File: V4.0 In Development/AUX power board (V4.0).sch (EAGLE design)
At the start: 75 parts, among them U1 ATMEGA328P_TQFP, U2 TPS5405DR

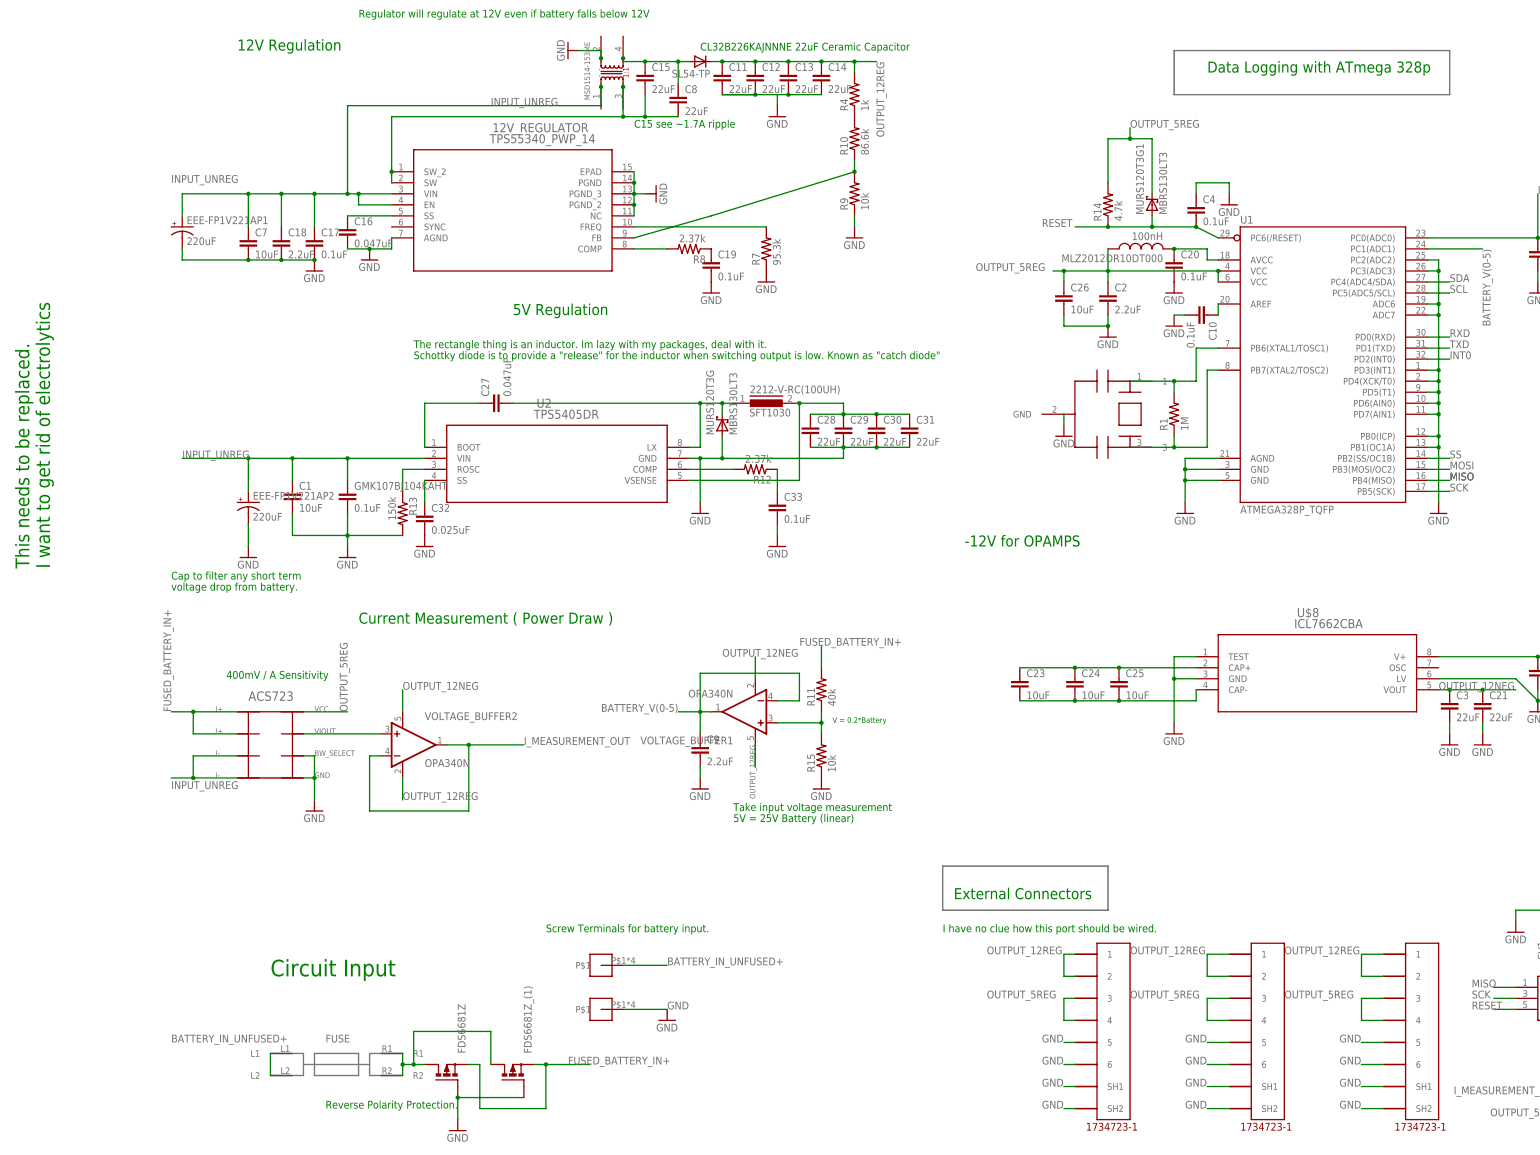
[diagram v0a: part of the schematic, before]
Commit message: Using nMOS reverse polarity protection
-added a cheaper 10uH inductor to the 5V supply
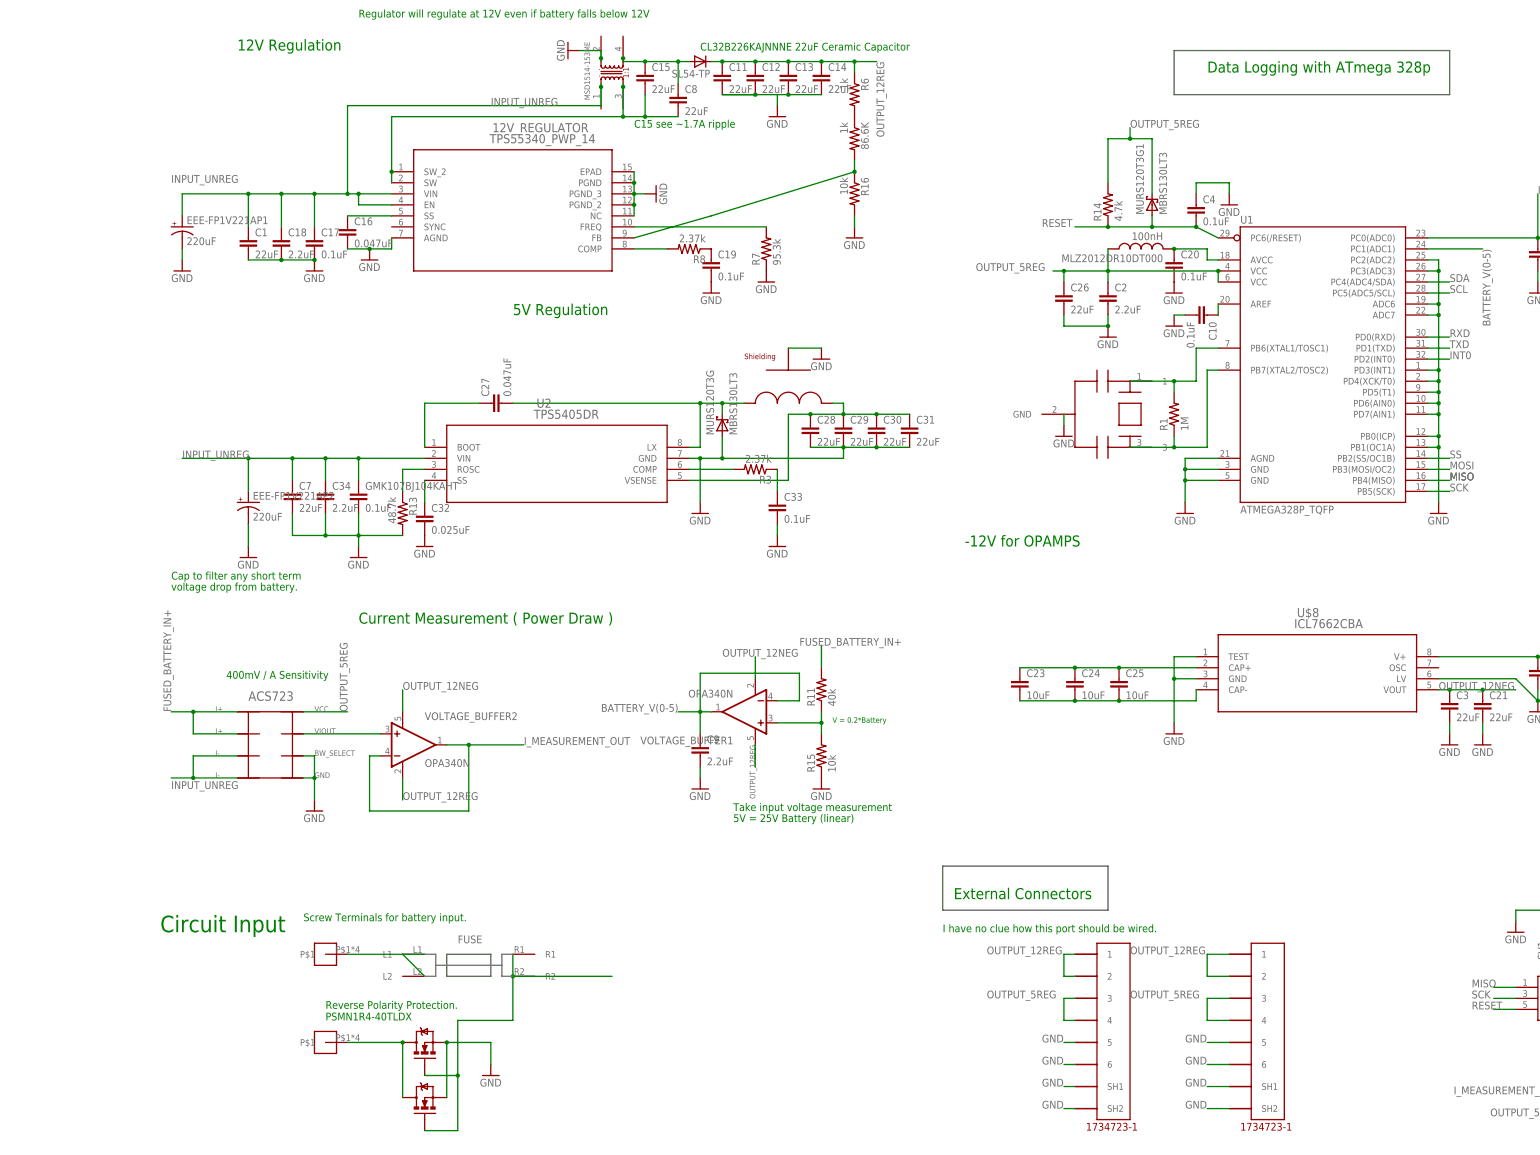
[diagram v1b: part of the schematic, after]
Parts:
- removed 2212-V-RC(100UH): SFT1030, inductors:SFT1030
- removed FDS6681Z, FDS6681Z_(1): (no value), transistor-power:P-MOSFET-SO8
- removed R10: 86.6k, resistor:R-US_R0603
- removed R4: 1k, resistor:R-US_R0603
- removed R9: 10k, resistor:R-US_R0603
- added 86.6K, R6: 1k, resistor:R-US_R0805
- added C34: 2.2uF, rcl:C-EUC0603
- added PSMN1R4-40TLDX, Q2: MOSFET-NCHANNELFDS6630A, PSMN1R4-40YLDX:MOSFET-NCHANNELFDS6630A
- added R16: 10k, resistor:R-US_R0805
- C1, C26, C7: value 10uF -> 22uF; device rcl:C-EUC0805 -> rcl:C-EUC1210
- R13: value 150k -> 48.7k
- U$5: value 5555140-6 -> CDEP147NP-100MC-125; device 5555140-6 RJ11:5555140-6 -> CDEP147NP-100MC-125:CDEP147NP-100MC-125
- renumbered R12 to R3
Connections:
- removed net MMM: FDS6681Z.D, FDS6681Z_(1).D, MINIBLADE.R1, MINIBLADE.R2
- removed net N$17: 2212-V-RC(100UH).2, C28.1, C29.1, C30.1, C31.1, U2.VSENSE
- new net N$22: PSMN1R4-40TLDX.D, Q2.D, U$7.P$1
- new net N$25: MINIBLADE.R1, MINIBLADE.R2, PSMN1R4-40TLDX.G, Q2.G
- new net N$26: C28.1, C29.1, C30.1, C31.1, U$5.PIN2, U2.VSENSE
- net FUSED_BATTERY_IN+: no longer FDS6681Z.S, FDS6681Z_(1).S
- net GND: now also C34.2, PSMN1R4-40TLDX.S, Q2.S, R16.2, U$5.GND; no longer FDS6681Z.G, FDS6681Z_(1).G, R9.1, U$5.5, U$5.6, U$5.SH1, U$5.SH2, U$7.P$1
- net INPUT_UNREG: now also C34.1
- net N$15: now also 86.6K.2, R16.1; no longer R10.1, R9.2
- net N$3: now also 86.6K.1, R6.2; no longer R10.2, R4.1
- net N$7: now also U$5.PIN1; no longer 2212-V-RC(100UH).1
- net OUTPUT_12REG: now also R6.1; no longer R4.2, U$5.1, U$5.2
- net OUTPUT_5REG: no longer U$5.3, U$5.4
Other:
- note added: "Reverse Polarity Protection. PSMN1R4-40TLDX"
- note removed: "Reverse Polarity Protection."
- note removed: "Schottky diode is to provide a "release" for the inductor when switching output is low. Known as "catch diode""
- note removed: "The rectangle thing is an inductor. Im lazy with my packages, deal with it."
- note removed: "This needs to be replaced. I want to get rid of electrolytics"
- moved on the sheet: C1, C7, GMK107BJ104KAHT

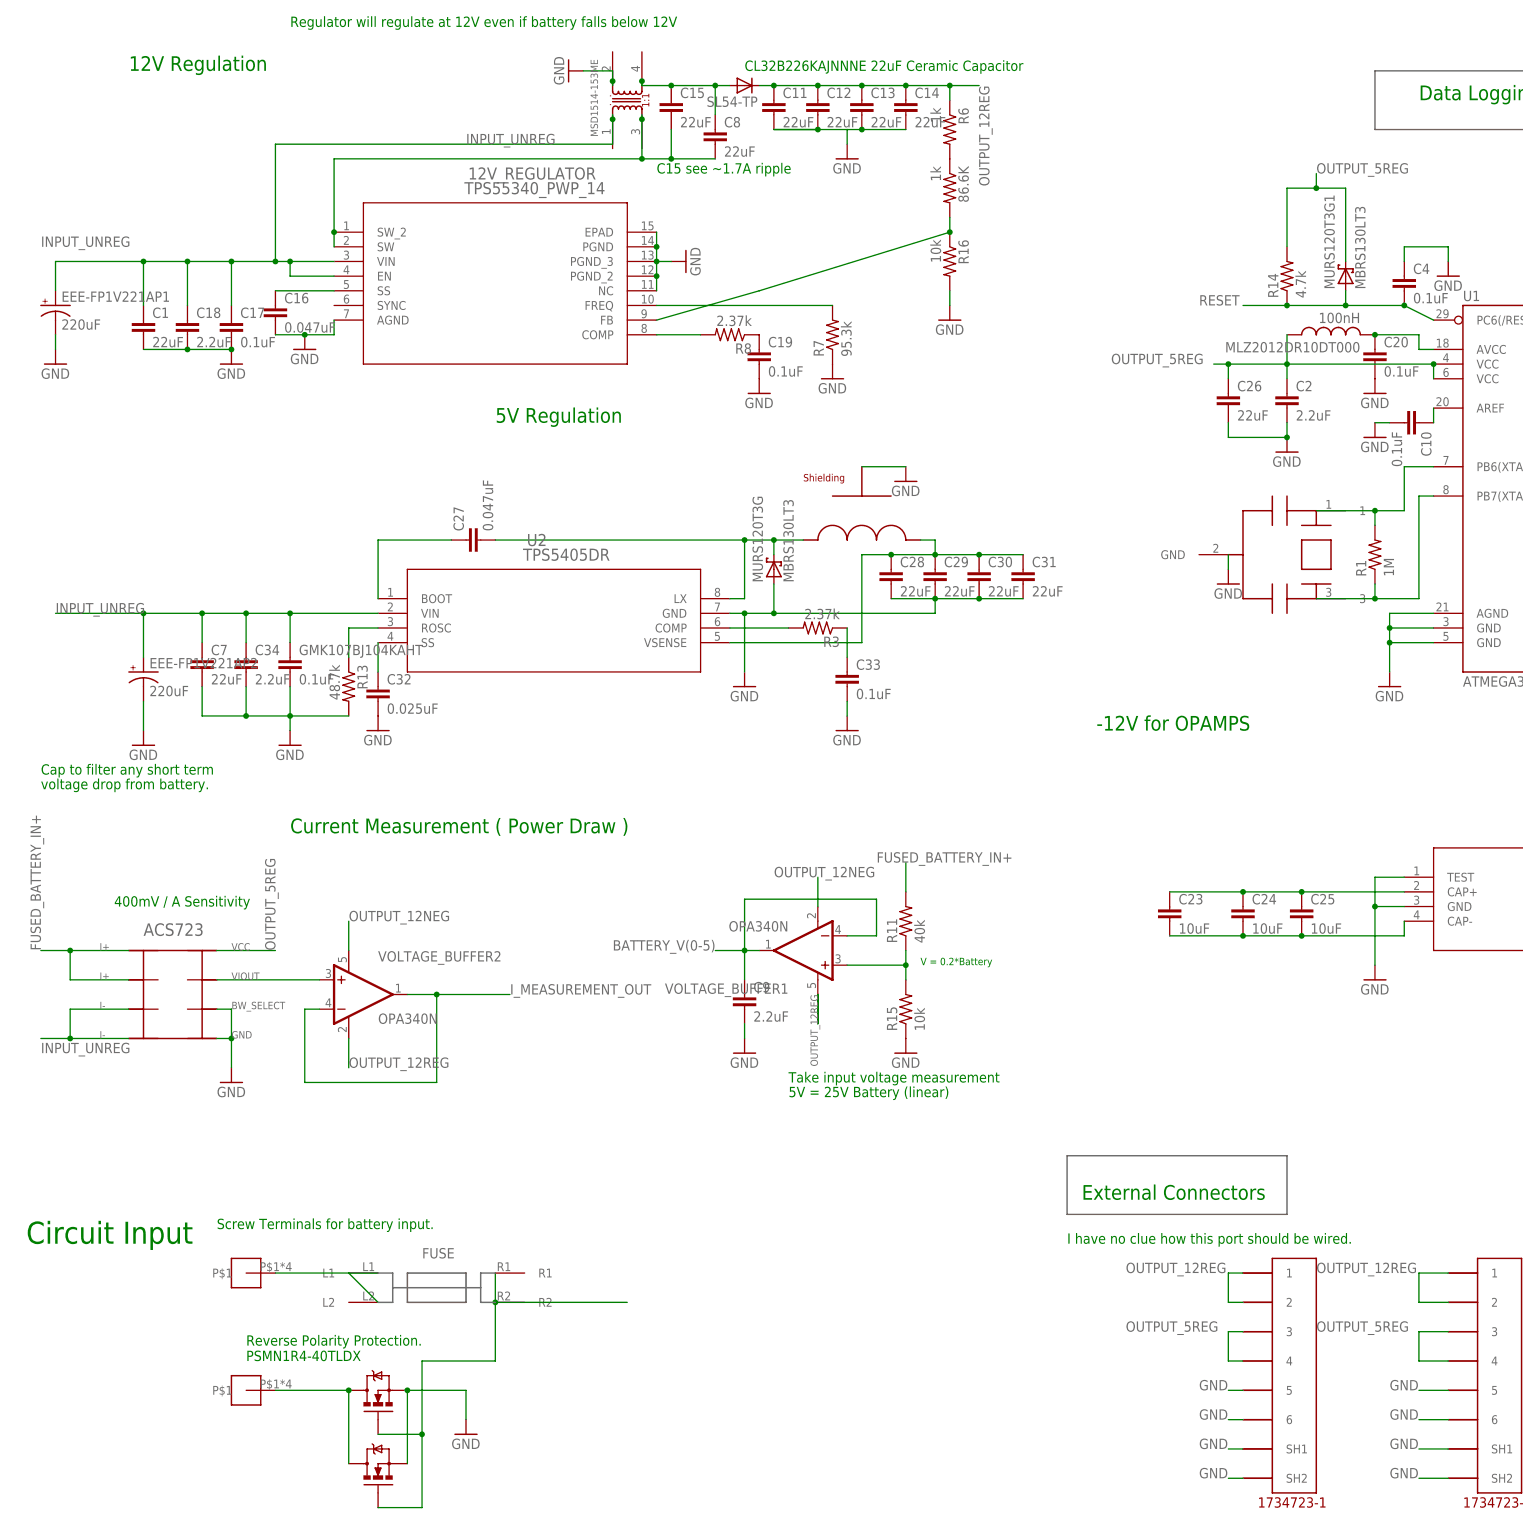
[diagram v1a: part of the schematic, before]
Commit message: New circuit protection
-40V- 60V protection.

LED indication for blown fuse and reverse polarity.

operates 8V- 18V
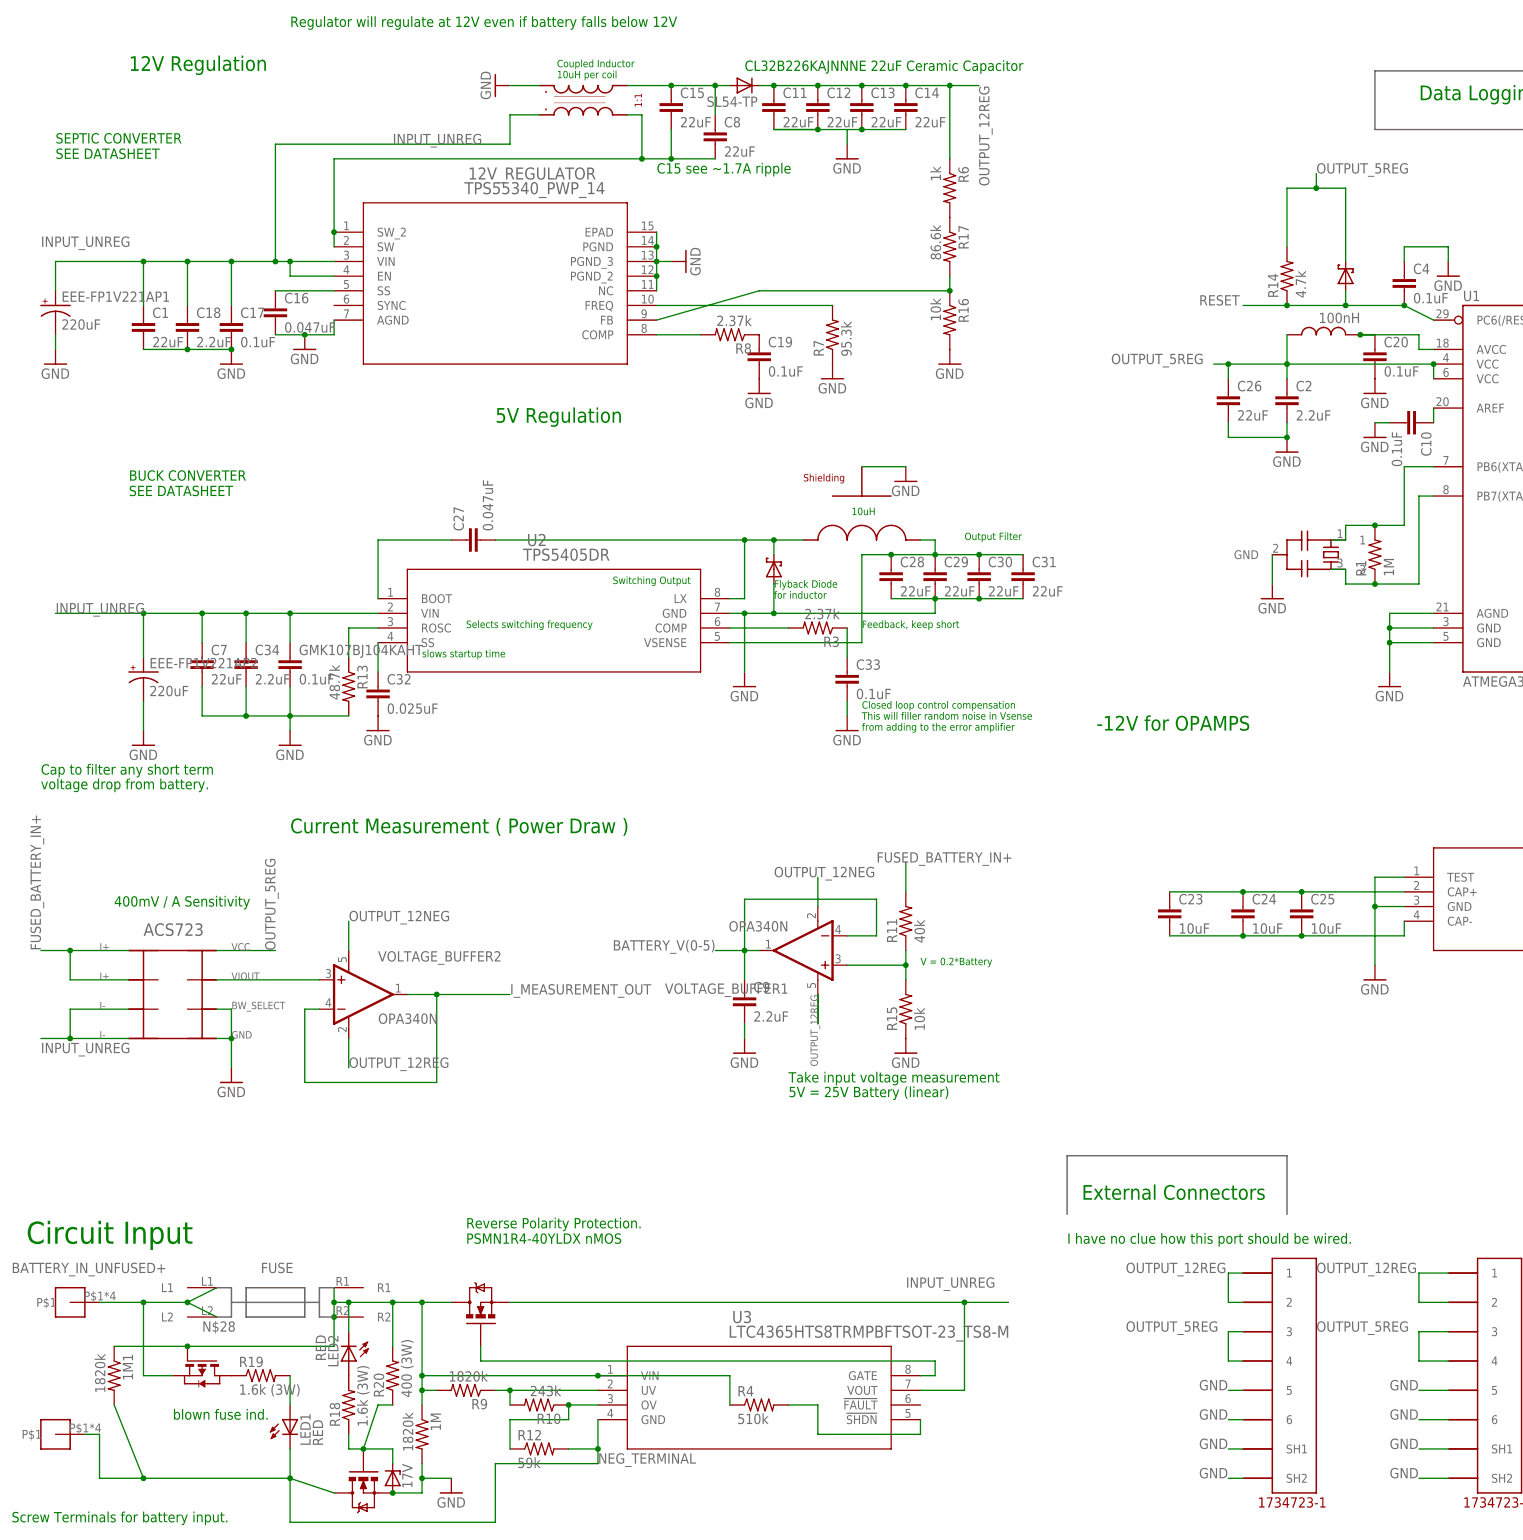
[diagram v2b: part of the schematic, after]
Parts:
- removed 86.6K: 1k, resistor:R-US_R0805
- removed MSD1514-153ME: MSD1514, MSD1514:MSD1514
- removed Q2: MOSFET-NCHANNELFDS6630A, PSMN1R4-40YLDX:MOSFET-NCHANNELFDS6630A
- added 1M, 1M1, R9: 1820k, rcl:R-US_R0805
- added LED1, LED2: RED, E-P-008-R1.2:LEDSML1206
- added PSMN1R4-40TLDX1: MOSFET-NCHANNELFDS6630A, PSMN1R4-40YLDX:MOSFET-NCHANNELFDS6630A
- added R10: 243k, rcl:R-US_R0805
- added R12: 59k, rcl:R-US_R0805
- added R17: 86.6k, resistor:R-US_R0805
- added R18, R19: 1.6k (3W), resistor:R-US_R2512
- added R20: 400 (3W), resistor:R-US_R2512
- added R4: 510k, rcl:R-US_R0805
- added TN2540-600G-TR: 17V, diode:ZENER-DIODEDO41Z10
- added U$9: 744873100, 744873100:744873100
- added U3: LTC4365HTS8TRMPBFTSOT-23_TS8-M, LTC4365:LTC4365HTS8TRMPBFTSOT-23_TS8-M
- added ZVP4525E6TA_1: MOSFET-PCHANNELFDS6675, zetex:PMOSSOT23-6
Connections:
- removed net N$22: PSMN1R4-40TLDX.D, Q2.D, U$7.P$1
- new net N$17: R19.1, ZVP4525E6TA_1.D
- new net N$19: PSMN1R4-40TLDX1.G, R18.1, R20.1, TN2540-600G-TR.C
- new net N$28: 1M.1, 1M1.1, LED2.C, MINIBLADE.R1, MINIBLADE.R2, PSMN1R4-40TLDX.D, R20.2, R4.1, R9.2, U3.VIN, ZVP4525E6TA_1.G
- new net N$29: R10.2, R9.1, U3.UV
- new net N$30: R10.1, R12.1, U3.OV
- new net N$31: R4.2, U3.!SHDN
- new net N$32: LED2.A, R18.2
- new net N$33: PSMN1R4-40TLDX.G, U3.GATE
- new net NEG_TERMINAL: 1M1.2, LED1.C, PSMN1R4-40TLDX1.D, R12.2, U$7.P$1, U3.GND
- net BATTERY_IN_UNFUSED+: now also ZVP4525E6TA_1.S
- net GND: now also 1M.2, PSMN1R4-40TLDX1.S, TN2540-600G-TR.A, U$9.L1_A; no longer MSD1514-153ME.2, PSMN1R4-40TLDX.S, Q2.S
- net INPUT_UNREG: now also PSMN1R4-40TLDX.S, U$9.L2_A, U3.VOUT; no longer MSD1514-153ME.1
- net N$15: now also R17.2; no longer 86.6K.2
- net N$25: now also LED1.A, R19.2; no longer MINIBLADE.R1, MINIBLADE.R2, PSMN1R4-40TLDX.G, Q2.G
- net N$3: now also R17.1; no longer 86.6K.1
- net N$4: now also U$9.L2_B; no longer MSD1514-153ME.3
- net N$6: now also U$9.L1_B; no longer MSD1514-153ME.4
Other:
- note added: "10uH"
- note added: "BUCK CONVERTER SEE DATASHEET"
- note added: "Closed loop control compensation This will filler random noise in Vsense from adding to the error amplifier"
- note added: "Coupled Inductor 10uH per coil"
- note added: "Feedback, keep short"
- note added: "Flyback Diode for inductor"
- note added: "Output Filter"
- note added: "Reverse Polarity Protection. PSMN1R4-40YLDX nMOS"
- note added: "SEPTIC CONVERTER SEE DATASHEET"
- note added: "Selects switching frequency"
- note added: "Switching Output"
- note added: "blown fuse ind."
- note added: "slows startup time"
- note removed: "Reverse Polarity Protection. PSMN1R4-40TLDX"
- moved on the sheet: R16, R6
